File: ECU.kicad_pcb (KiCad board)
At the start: 4 copper layers, 132 x 119 mm, 124 parts, among them J1 Solenoid 0, J10 Thermocouple 3, J13 External SPI, J14 External UART, J15 External I2C, J16 Pressure Transducer 0, J17 Pressure Transducer 1, J18 Pressure Transducer 2, J19 Pressure Transducer 3, J2 Solenoid 1, J20 Pressure Transducer 4, J21 Pressure Transducer 5, J22 Power In, J3 Solenoid 2, J4 Solenoid 3, J5 Solenoid 4, J6 Solenoid 5, J7 Thermocouple 0, J8 Thermocouple 1, J9 Thermocouple 2, U1 Teensy4.1, U10 MAX31855, U11 MAX31855, U12 OPA357, U13 OPA357, U14 OPA357, U15 OPA357, U16 OPA357, U17 OPA357, U18 uA7824, U19 uA7824, U2 OPA357, U20 uA7805, U21 TLV2217, U3 OPA357, U4 OPA357, U5 OPA357, U6 OPA357, U7 OPA357, U8 MAX31855, U9 MAX31855

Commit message: Add logo to silkscreen
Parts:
- added G***: LOGO, ECU:UCIRP-logo, F.Cu at (129.0, 114.0)

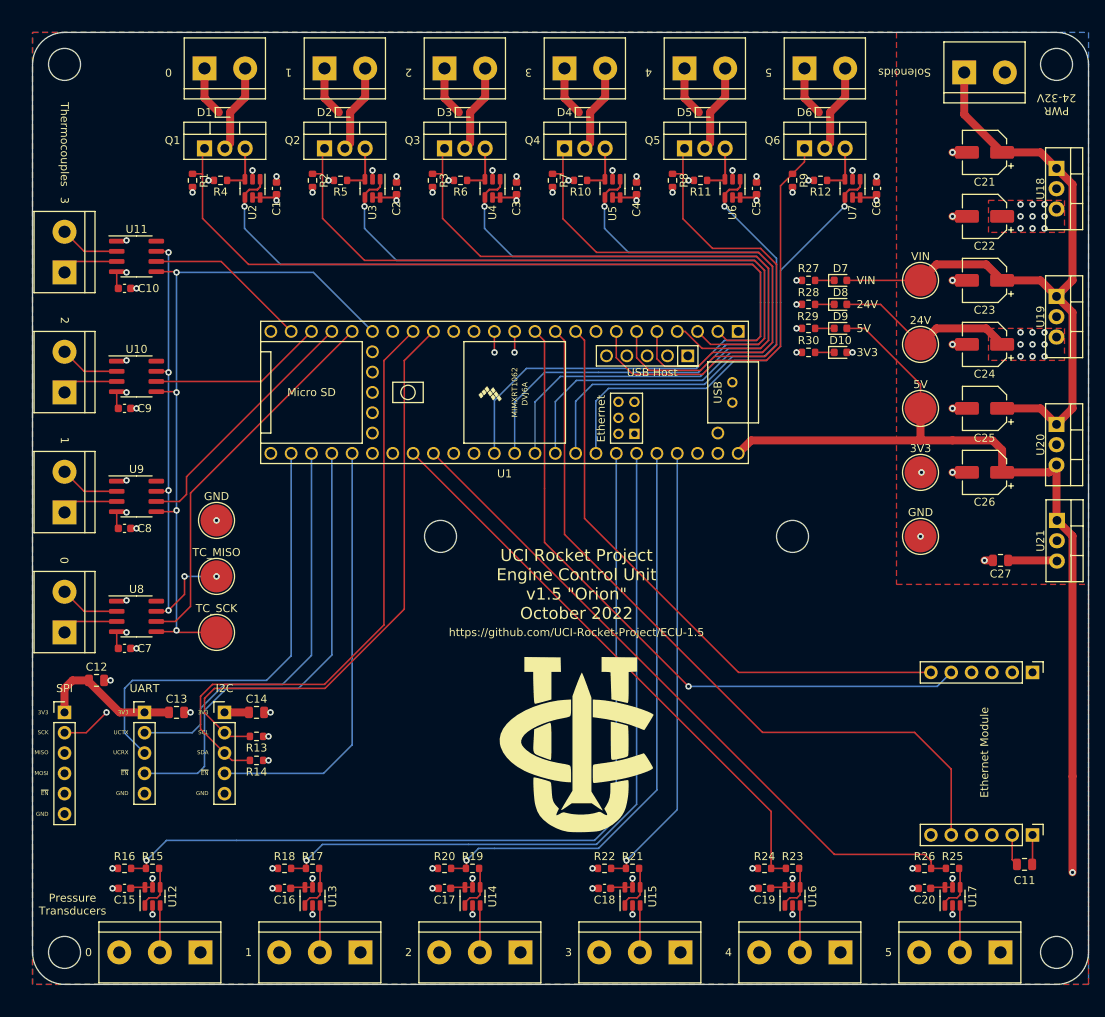
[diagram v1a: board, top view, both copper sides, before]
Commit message: Add silkscreen labels for screw terminals
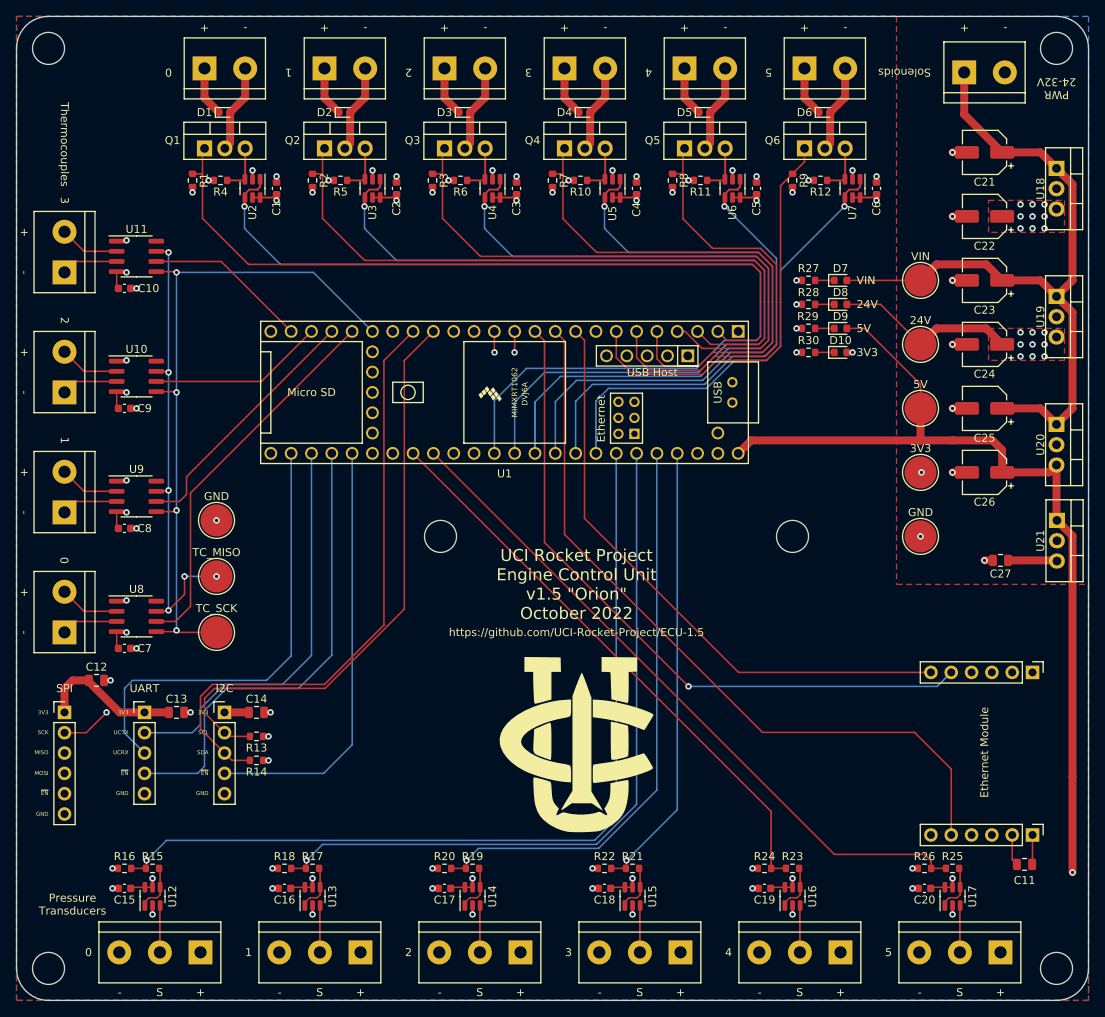
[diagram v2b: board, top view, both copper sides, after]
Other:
- board size 132 x 119 mm -> 134 x 123 mm
- board text added: "+"
- board text added: "-"
- board text added: "S"
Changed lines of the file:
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@@
     )
   )
-  (gr_circle (center 65 140) (end 67 140) (layer "Edge.Cuts") (width 0.1) (fill none))
+  (gr_circle (center 63 142) (end 65 142) (layer "Edge.Cuts") (width 0.1) (fill none))
   (gr_circle (center 112 88) (end 114 88) (layer "Edge.Cuts") (width 0.1) (fill none))
-  (gr_circle (center 189 29) (end 191 29) (layer "Edge.Cuts") (width 0.1) (fill none))
-  (gr_arc (start 193 140) (mid 191.828427 142.828427) (end 189 144) (layer "Edge.Cuts") (width 0.1))
-  (gr_circle (center 65 29) (end 67 29) (layer "Edge.Cuts") (width 0.1) (fill none))
-  (gr_circle (center 189 140) (end 191 140) (layer "Edge.Cuts") (width 0.1) (fill none))
-  (gr_line (start 193 29) (end 193 140) (layer "Edge.Cuts") (width 0.1))
-  (gr_line (start 189 144) (end 65 144) (layer "Edge.Cuts") (width 0.1))
-  (gr_line (start 65 25) (end 189 25) (layer "Edge.Cuts") (width 0.1))
-  (gr_arc (start 61 29) (mid 62.171573 26.171573) (end 65 25) (layer "Edge.Cuts") (width 0.1))
-  (gr_arc (start 65 144) (mid 62.171573 142.828427) (end 61 140) (layer "Edge.Cuts") (width 0.1))
-  (gr_arc (start 189 25) (mid 191.828427 26.171573) (end 193 29) (layer "Edge.Cuts") (width 0.1))
-  (gr_line (start 61 29) (end 61 140) (layer "Edge.Cuts") (width 0.1))
+  (gr_circle (center 189 27) (end 191 27) (layer "Edge.Cuts") (width 0.1) (fill none))
+  (gr_arc (start 193 142) (mid 191.828427 144.828427) (end 189 146) (layer "Edge.Cuts") (width 0.1))
+  (gr_circle (center 63 27) (end 65 27) (layer "Edge.Cuts") (width 0.1) (fill none))
+  (gr_circle (center 189 142) (end 191 142) (layer "Edge.Cuts") (width 0.1) (fill none))
+  (gr_line (start 193 27) (end 193 142) (layer "Edge.Cuts") (width 0.1))
+  (gr_line (start 189 146) (end 63 146) (layer "Edge.Cuts") (width 0.1))
+  (gr_line (start 63 23) (end 189 23) (layer "Edge.Cuts") (width 0.1))
+  (gr_arc (start 59 27) (mid 60.171573 24.171573) (end 63 23) (layer "Edge.Cuts") (width 0.1))
+  (gr_arc (start 63 146) (mid 60.171573 144.828427) (end 59 142) (layer "Edge.Cuts") (width 0.1))
+  (gr_arc (start 189 23) (mid 191.828427 24.171573) (end 193 27) (layer "Edge.Cuts") (width 0.1))
+  (gr_line (start 59 27) (end 59 142) (layer "Edge.Cuts") (width 0.1))
   (gr_circle (center 156 88) (end 158 88) (layer "Edge.Cuts") (width 0.1) (fill none))
+  (gr_text "+" (at 177.5 24.5 180) (layer "F.SilkS")
+    (effects (font (size 1 1) (thickness 0.15)))
+  )
+  (gr_text "S" (at 136.9 145) (layer "F.SilkS")
+    (effects (font (size 1 1) (thickness 0.15)))
+  )
   (gr_text "1" (at 88 140) (layer "F.SilkS")
+    (effects (font (size 1 1) (thickness 0.15)))
+  )
+  (gr_text "S" (at 116.9 145) (layer "F.SilkS")
     (effects (font (size 1 1) (thickness 0.15)))
   )
@@
     (effects (font (size 0.5 0.5) (thickness 0.1)) (justify right))
   )
+  (gr_text "+" (at 82.5 24.5 180) (layer "F.SilkS")
+    (effects (font (size 1 1) (thickness 0.15)))
+  )
+  (gr_text "-" (at 171.9 145) (layer "F.SilkS")
+    (effects (font (size 1 1) (thickness 0.15)))
+  )
+  (gr_text "-" (at 162.6 24.5 180) (layer "F.SilkS")
+    (effects (font (size 1 1) (thickness 0.15)))
+  )
+  (gr_text "+" (at 82 145) (layer "F.SilkS")
+    (effects (font (size 1 1) (thickness 0.15)))
+  )
+  (gr_text "-" (at 102.6 24.5 180) (layer "F.SilkS")
+    (effects (font (size 1 1) (thickness 0.15)))
+  )
+  (gr_text "+" (at 60 80 270) (layer "F.SilkS")
+    (effects (font (size 1 1) (thickness 0.15)))
+  )
   (gr_text "3V3" (at 172 77) (layer "F.SilkS")
     (effects (font (size 1 1) (thickness 0.15)))
   )
-  (gr_text "PWR\n24-32V" (at 189 34 180) (layer "F.SilkS")
+  (gr_text "-" (at 60 55 270) (layer "F.SilkS")
+    (effects (font (size 1 1) (thickness 0.15)))
+  )
+  (gr_text "PWR\n24-32V" (at 189 32 180) (layer "F.SilkS")
     (effects (font (size 1 1) (thickness 0.15)))
   )
@@
     (effects (font (size 1 1) (thickness 0.15)))
   )
+  (gr_text "-" (at 151.9 145) (layer "F.SilkS")
+    (effects (font (size 1 1) (thickness 0.15)))
+  )
+  (gr_text "S" (at 76.9 145) (layer "F.SilkS")
+    (effects (font (size 1 1) (thickness 0.15)))
+  )
+  (gr_text "-" (at 131.9 145) (layer "F.SilkS")
+    (effects (font (size 1 1) (thickness 0.15)))
+  )
   (gr_text "3" (at 65 46 270) (layer "F.SilkS")
     (effects (font (size 1 1) (thickness 0.15)))
   )
+  (gr_text "+" (at 157.5 24.5 180) (layer "F.SilkS")
+    (effects (font (size 1 1) (thickness 0.15)))
+  )
   (gr_text "GND" (at 73 120.1) (layer "F.SilkS")
     (effects (font (size 0.5 0.5) (thickness 0.1)) (justify right))
   )
+  (gr_text "+" (at 97.5 24.5 180) (layer "F.SilkS")
+    (effects (font (size 1 1) (thickness 0.15)))
+  )
   (gr_text "5V" (at 172 69) (layer "F.SilkS")
     (effects (font (size 1 1) (thickness 0.15)))
   )
+  (gr_text "+" (at 102 145) (layer "F.SilkS")
+    (effects (font (size 1 1) (thickness 0.15)))
+  )
+  (gr_text "-" (at 182.6 24.5 180) (layer "F.SilkS")
+    (effects (font (size 1 1) (thickness 0.15)))
+  )
+  (gr_text "+" (at 162 145) (layer "F.SilkS")
+    (effects (font (size 1 1) (thickness 0.15)))
+  )
   (gr_text "Pressure\nTransducers" (at 66 134) (layer "F.SilkS")
     (effects (font (size 1 1) (thickness 0.15)))
@@
     (effects (font (size 1 1) (thickness 0.15)))
   )
+  (gr_text "+" (at 127.5 24.5 180) (layer "F.SilkS")
+    (effects (font (size 1 1) (thickness 0.15)))
+  )
   (gr_text "VIN" (at 172 53) (layer "F.SilkS")
     (effects (font (size 1 1) (thickness 0.15)))
@@
     (effects (font (size 0.5 0.5) (thickness 0.1)) (justify right))
   )
+  (gr_text "+" (at 60 50 270) (layer "F.SilkS")
+    (effects (font (size 1 1) (thickness 0.15)))
+  )
+  (gr_text "+" (at 122 145) (layer "F.SilkS")
+    (effects (font (size 1 1) (thickness 0.15)))
+  )
   (gr_text "1" (at 93 30 180) (layer "F.SilkS")
     (effects (font (size 1 1) (thickness 0.15)))
   )
+  (gr_text "+" (at 112.5 24.5 180) (layer "F.SilkS")
+    (effects (font (size 1 1) (thickness 0.15)))
+  )
   (gr_text "Thermocouples" (at 65 39 270) (layer "F.SilkS")
     (effects (font (size 1 1) (thickness 0.15)))
@@
   )
   (gr_text "24V" (at 172 61) (layer "F.SilkS")
+    (effects (font (size 1 1) (thickness 0.15)))
+  )
+  (gr_text "S" (at 176.9 145) (layer "F.SilkS")
     (effects (font (size 1 1) (thickness 0.15)))
   )
@@
     (effects (font (size 0.5 0.5) (thickness 0.1)) (justify right))
   )
+  (gr_text "-" (at 111.9 145) (layer "F.SilkS")
+    (effects (font (size 1 1) (thickness 0.15)))
+  )
+  (gr_text "-" (at 87.6 24.5 180) (layer "F.SilkS")
+    (effects (font (size 1 1) (thickness 0.15)))
+  )
+  (gr_text "-" (at 91.9 145) (layer "F.SilkS")
+    (effects (font (size 1 1) (thickness 0.15)))
+  )
+  (gr_text "+" (at 142.5 24.5 180) (layer "F.SilkS")
+    (effects (font (size 1 1) (thickness 0.15)))
+  )
+  (gr_text "-" (at 60 100 270) (layer "F.SilkS")
+    (effects (font (size 1 1) (thickness 0.15)))
+  )
+  (gr_text "S" (at 96.9 145) (layer "F.SilkS")
+    (effects (font (size 1 1) (thickness 0.15)))
+  )
   (gr_text "3" (at 123 30 180) (layer "F.SilkS")
     (effects (font (size 1 1) (thickness 0.15)))
@@
   )
   (gr_text "TC_SCK" (at 84 97) (layer "F.SilkS")
+    (effects (font (size 1 1) (thickness 0.15)))
+  )
+  (gr_text "-" (at 132.6 24.5 180) (layer "F.SilkS")
+    (effects (font (size 1 1) (thickness 0.15)))
+  )
+  (gr_text "+" (at 60 65 270) (layer "F.SilkS")
     (effects (font (size 1 1) (thickness 0.15)))
   )
@@
     (effects (font (size 1 1) (thickness 0.15)))
   )
+  (gr_text "-" (at 60 70 270) (layer "F.SilkS")
+    (effects (font (size 1 1) (thickness 0.15)))
+  )
+  (gr_text "+" (at 182 145) (layer "F.SilkS")
+    (effects (font (size 1 1) (thickness 0.15)))
+  )
   (gr_text "GND" (at 172 85) (layer "F.SilkS")
+    (effects (font (size 1 1) (thickness 0.15)))
+  )
+  (gr_text "+" (at 142 145) (layer "F.SilkS")
+    (effects (font (size 1 1) (thickness 0.15)))
+  )
+  (gr_text "S" (at 156.9 145) (layer "F.SilkS")
     (effects (font (size 1 1) (thickness 0.15)))
   )
@@
     (effects (font (size 1 1) (thickness 0.15)))
   )
+  (gr_text "-" (at 60 85 270) (layer "F.SilkS")
+    (effects (font (size 1 1) (thickness 0.15)))
+  )
+  (gr_text "+" (at 60 95 270) (layer "F.SilkS")
+    (effects (font (size 1 1) (thickness 0.15)))
+  )
   (gr_text "SCK" (at 63 112.5) (layer "F.SilkS")
     (effects (font (size 0.5 0.5) (thickness 0.1)) (justify right))
@@
     (effects (font (size 0.5 0.5) (thickness 0.1)) (justify right))
   )
+  (gr_text "-" (at 147.6 24.5 180) (layer "F.SilkS")
+    (effects (font (size 1 1) (thickness 0.15)))
+  )
   (gr_text "3V3" (at 63 110) (layer "F.SilkS")
     (effects (font (size 0.5 0.5) (thickness 0.1)) (justify right))
+  )
+  (gr_text "-" (at 71.9 145) (layer "F.SilkS")
+    (effects (font (size 1 1) (thickness 0.15)))
+  )
+  (gr_text "-" (at 117.6 24.5 180) (layer "F.SilkS")
+    (effects (font (size 1 1) (thickness 0.15)))
   )
   (gr_text "0" (at 68 140) (layer "F.SilkS")
@@
         (xy 169 94)
         (xy 193 94)
-        (xy 193 144)
-        (xy 61 144)
-        (xy 61 25)
-        (xy 169 25)
+        (xy 193 146)
+        (xy 59 146)
+        (xy 59 23)
+        (xy 169 23)
       )
     )
@@
     (polygon
       (pts
-        (xy 193 144)
-        (xy 61 144)
-        (xy 61 25)
-        (xy 193 25)
+        (xy 193 146)
+        (xy 59 146)
+        (xy 59 23)
+        (xy 193 23)
       )
     )
@@
         (xy 67 134)
         (xy 193 134)
-        (xy 193 144)
-        (xy 61 144)
-        (xy 61 25)
-        (xy 193 25)
+        (xy 193 146)
+        (xy 59 146)
+        (xy 59 23)
+        (xy 193 23)
       )
     )
@@
     (polygon
       (pts
-        (xy 193 144)
-        (xy 61 144)
-        (xy 61 25)
-        (xy 193 25)
+        (xy 193 146)
+        (xy 59 146)
+        (xy 59 23)
+        (xy 193 23)
       )
     )

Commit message: Redesign power supply
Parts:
- removed C24, C25, C26: 10uF,50V, Capacitor_SMD:CP_Elec_5x5.9
- removed D8: LED, Diode_SMD:D_0603_1608Metric
- removed R28: 1.2K, Resistor_SMD:R_0603_1608Metric
- removed TP1, TP2: ~, TestPoint:TestPoint_Pad_D4.0mm
- removed U18, U19: uA7824, Package_TO_SOT_THT:TO-220-3_Vertical
- C21, C22, C23: value 10uF,50V -> 10uF; footprint Capacitor_SMD:CP_Elec_5x5.9 -> Capacitor_SMD:C_1206_3216Metric
- C27: value 22uF -> 10uF; footprint Capacitor_SMD:C_0805_2012Metric -> Capacitor_SMD:C_1206_3216Metric
- moved C23 33.8 mm to (169.0, 88.0)
- moved C21 32.0 mm to (169.0, 70.0)
- moved C22 29.2 mm to (169.0, 75.0)
- moved C27 13.2 mm to (169.0, 93.0)
- moved TP3 10.8 mm to (162.0, 76.0)
- moved TP4 10.8 mm to (162.0, 84.0)
- moved TP5 10.8 mm to (162.0, 92.0)
- moved U20 8.90 mm to (181.1, 70.0)
- moved U21 8.25 mm to (181.1, 88.0)
- moved D10 4.12 mm to (163.0, 61.0)
- moved D9 4.12 mm to (163.0, 58.0)
- moved R29 4.12 mm to (159.0, 58.0)
- moved R30 4.12 mm to (159.0, 61.0)
- moved D7 1.41 mm to (163.0, 55.0)
- moved R27 1.41 mm to (159.0, 55.0)
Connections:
- C21 pad 1: +28V -> +24V
- C22 pad 1: +24V -> +5V
- C23 pad 1: +28V -> +24V
- D7 pad 2: +28V -> +24V
- J22 pad 1: +28V -> +24V
- U20 pad 1: +28V -> +24V
- U21 pad 1: +5V -> +24V
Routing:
- net +28V: track 91.2 -> 0.00 mm
- net GND: track 62.8 -> 48.3 mm, vias 66 -> 54
- net +3V3: track 70.5 -> 75.5 mm
- net +24V: track 60.6 -> 64.8 mm, vias 18 -> 1
- net Net-(D8-Pad1): track 2.39 -> 0.00 mm
- net +5V: track 138.4 -> 140.1 mm
- removed copper zone on F.Cu, net +24V
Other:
- board text removed: "PWR 24-32V"
- board text removed: "VIN"

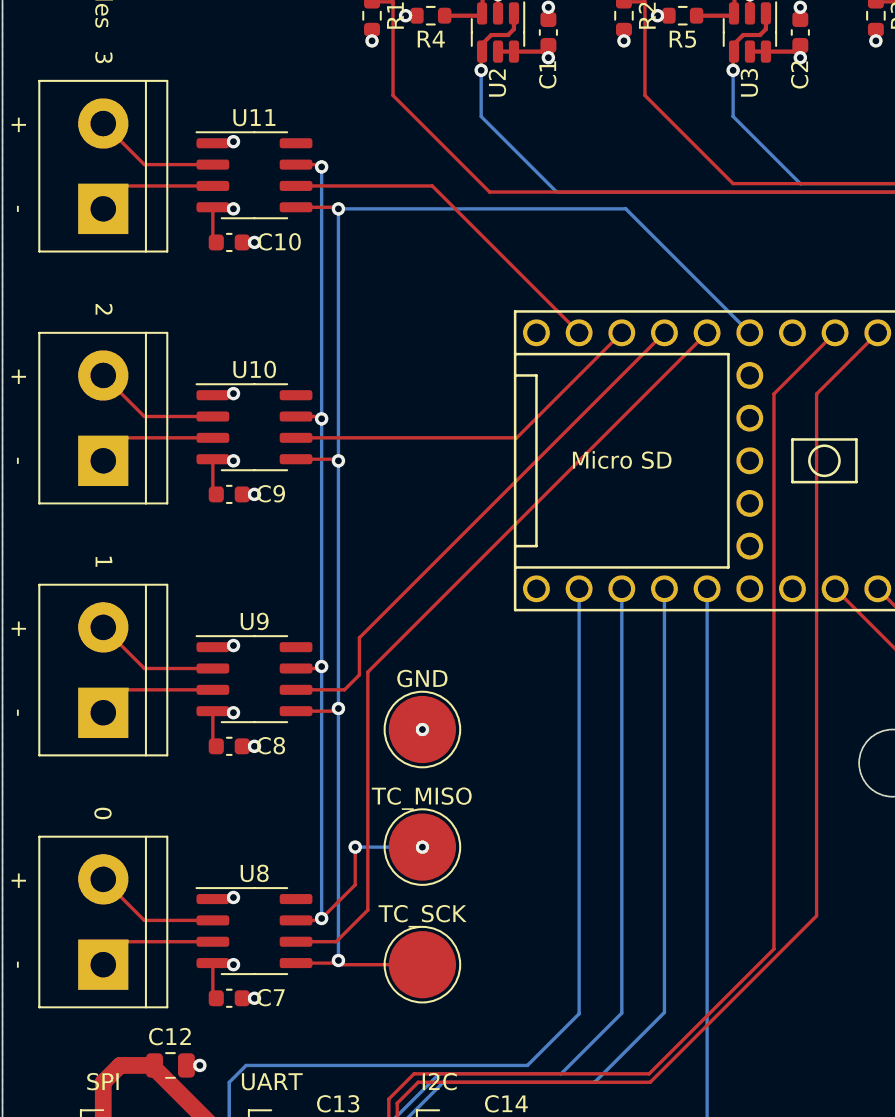
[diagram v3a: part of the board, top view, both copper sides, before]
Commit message: Add filter caps to TC input
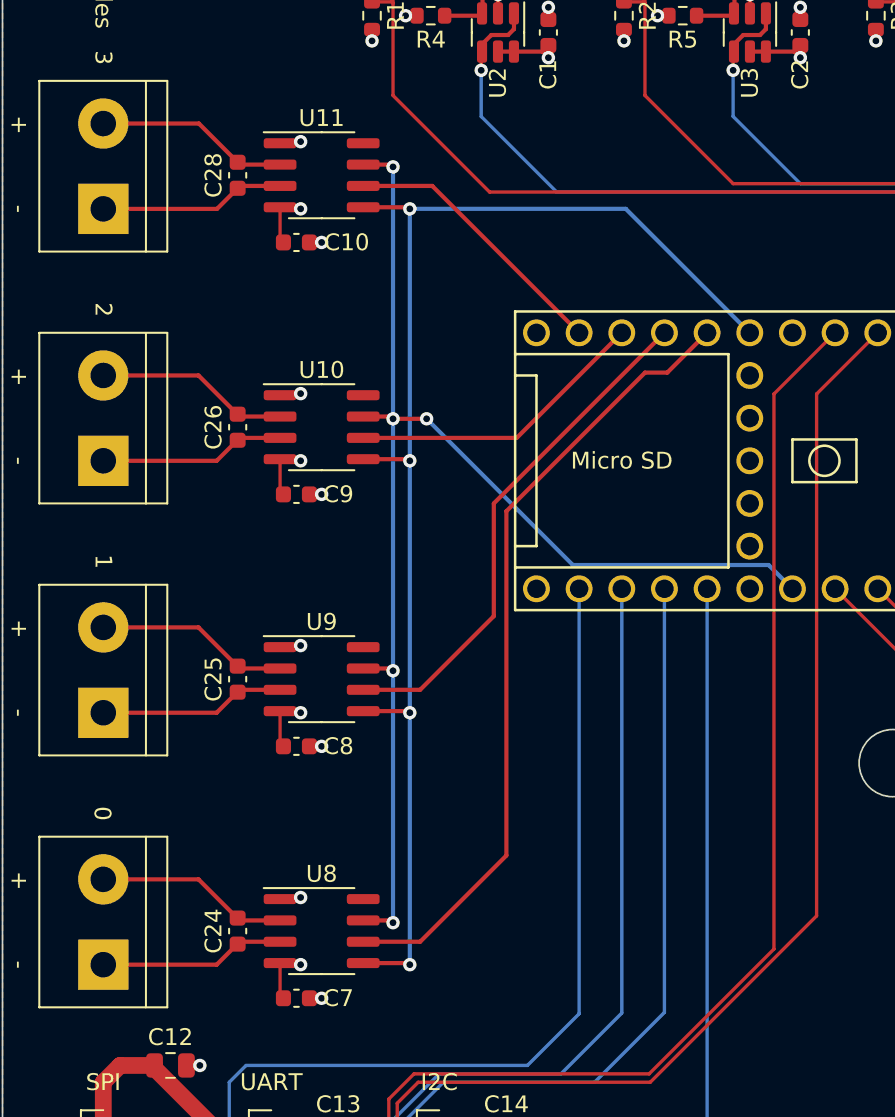
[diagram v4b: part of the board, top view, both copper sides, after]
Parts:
- removed TP6, TP7, TP8: ~, TestPoint:TestPoint_Pad_D4.0mm
- added C24: 10nF, Capacitor_SMD:C_0603_1608Metric, F.Cu at (73.0, 98.0)
- added C25: 10nF, Capacitor_SMD:C_0603_1608Metric, F.Cu at (73.0, 83.0)
- added C26: 10nF, Capacitor_SMD:C_0603_1608Metric, F.Cu at (73.0, 68.0)
- added C28: 10nF, Capacitor_SMD:C_0603_1608Metric, F.Cu at (73.0, 53.0)
- moved C10 4.00 mm to (76.5, 57.0)
- moved C7 4.00 mm to (76.5, 102.0)
- moved C8 4.00 mm to (76.5, 87.0)
- moved C9 4.00 mm to (76.5, 72.0)
- moved U10 4.00 mm to (78.0, 68.0)
- moved U11 4.00 mm to (78.0, 53.0)
- moved U8 4.00 mm to (78.0, 98.0)
- moved U9 4.00 mm to (78.0, 83.0)
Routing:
- net SPI_TC_MISO: track 91.3 -> 80.3 mm, vias 6 -> 5
- net SPI_TC_SCK: track 87.7 -> 79.6 mm
- net SPI_TC3_~{EN}: track 20.5 -> 16.5 mm
- net SPI_TC2_~{EN}: track 22.0 -> 18.0 mm
- net Net-(J9-Pad2): track 7.54 -> 11.5 mm
- net Net-(J9-Pad1): track 7.09 -> 11.1 mm
- net Net-(J8-Pad2): track 7.54 -> 11.5 mm
- net Net-(J8-Pad1): track 7.09 -> 11.1 mm
- net Net-(J10-Pad1): track 7.09 -> 11.1 mm
- net Net-(U8-Pad3): track 7.09 -> 11.1 mm
- net Net-(U8-Pad2): track 7.54 -> 11.5 mm
- net Net-(J10-Pad2): track 7.54 -> 11.5 mm
- net SPI_TC1_~{EN}: track 32.0 -> 30.7 mm
- net GND: vias 54 -> 53
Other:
- board text removed: "TC_MISO"
- board text removed: "TC_SCK"
